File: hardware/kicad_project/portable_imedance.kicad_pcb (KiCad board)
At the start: 4 copper layers, 48.3 x 40.9 mm, 62 parts, among them J1 UMC, J10 UMC, J11 UMC, J12 UMC, J13 UMC, J14 UMC, J15 UMC, J16 UMC, J17 Conn_02x12_Odd_Even, J19 Conn_02x06_Odd_Even, J2 UMC, J20 Conn_01x02, J21 Conn_01x02, J22 Conn_01x02, J23 Conn_01x02, J24 Conn_01x02, J25 Conn_01x02, J3 UMC, J4 UMC, J5 UMC, J6 UMC, J7 UMC, J8 UMC, J9 UMC, U2 AD5933, U3 ADG1209, U5 LD3985G25R_TSOT23, U6 OPA2836, U7 OPA2836, U8 AD8130, U9 ADG1209

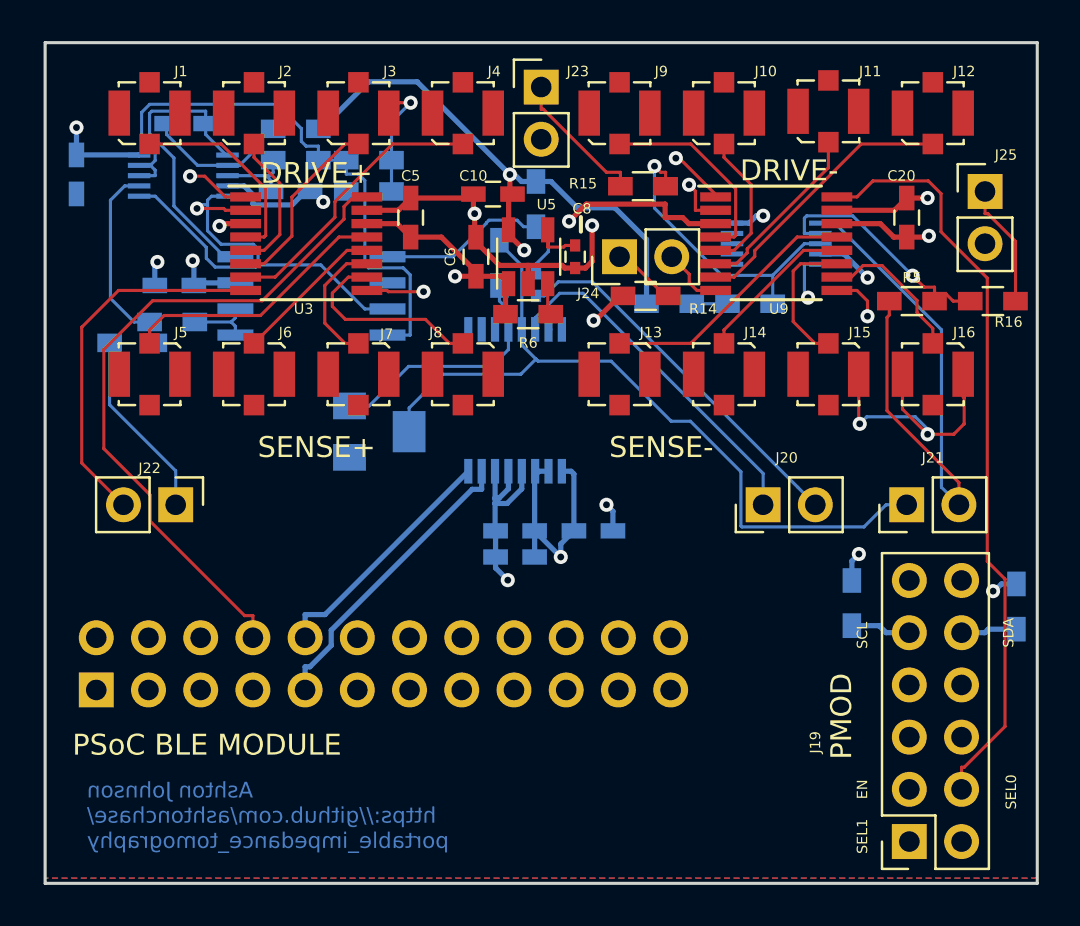
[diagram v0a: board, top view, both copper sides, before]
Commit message: updated board to include aux connector
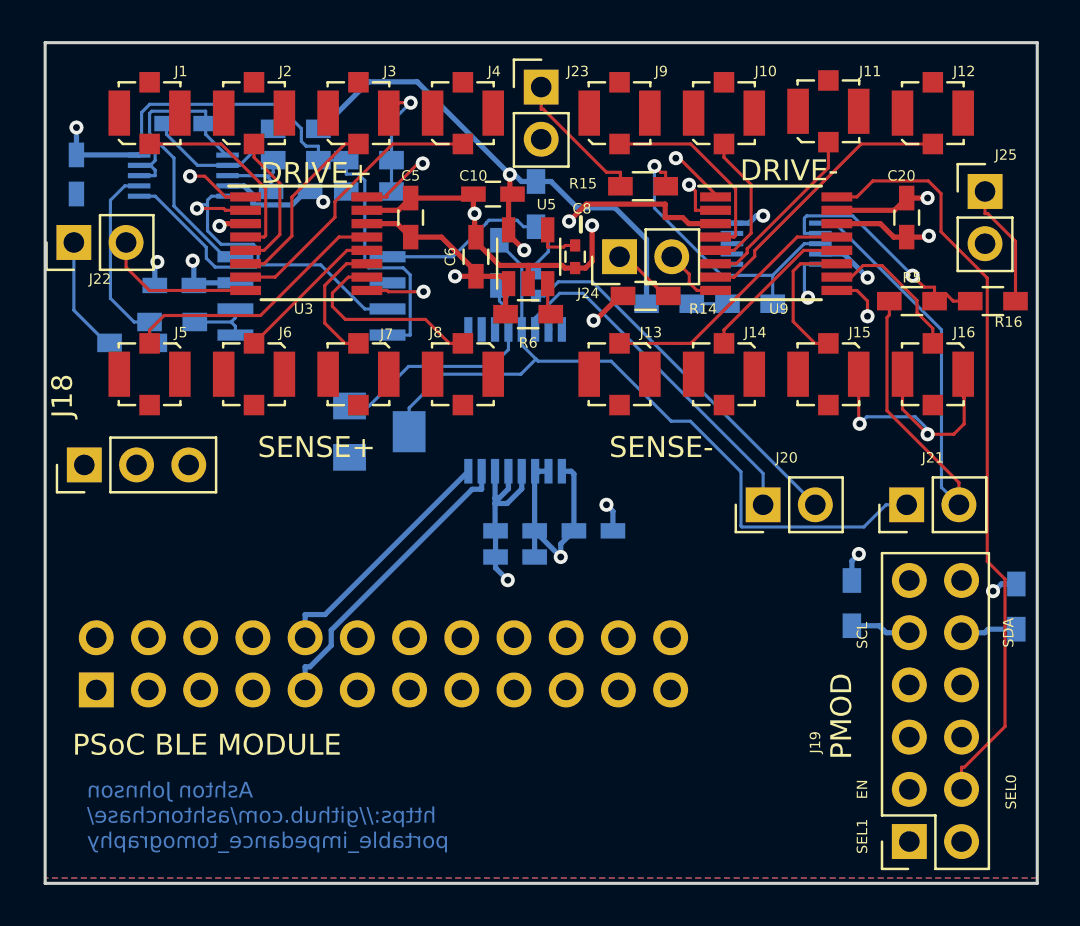
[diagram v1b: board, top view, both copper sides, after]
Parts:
- added J18: Conn_01x03, Socket_Strips:Socket_Strip_Straight_1x03_Pitch2.54mm, F.Cu at (95.9, 64.5)
- moved J22 13.7 mm to (95.4, 53.7), turned to 90 degrees
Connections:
- J17 pad 22: Net-(J17-Pad22) -> /Auxiliary Analog Connector/AIN
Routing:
- net /Auxiliary Analog Connector/AIN: track 0.00 -> 24.5 mm
- net /Receive Mux/DRIVE: track 18.2 -> 7.48 mm
- net /Cypress BLE Headers/SEL0: track 109.0 -> 114.5 mm, vias 0 -> 1
- net /Cypress BLE Headers/SEL1: track 94.2 -> 99.5 mm
- net /AD5933 Front End/DRIVE_P: track 9.21 -> 5.69 mm
